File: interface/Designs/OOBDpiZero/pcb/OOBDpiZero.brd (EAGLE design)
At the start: 73.5 x 42 mm, 120 parts, among them IC10 STM32F042CT, IC11 EEPROM24, IC20 GL850G-31, IC3 DS3231, IC4 MC34063-SO, Q2 12MHz, U1 SN65HVD230(SO8), U11 STM32F042CT, U2 SN65HVD230(SO8), U4 SY6280

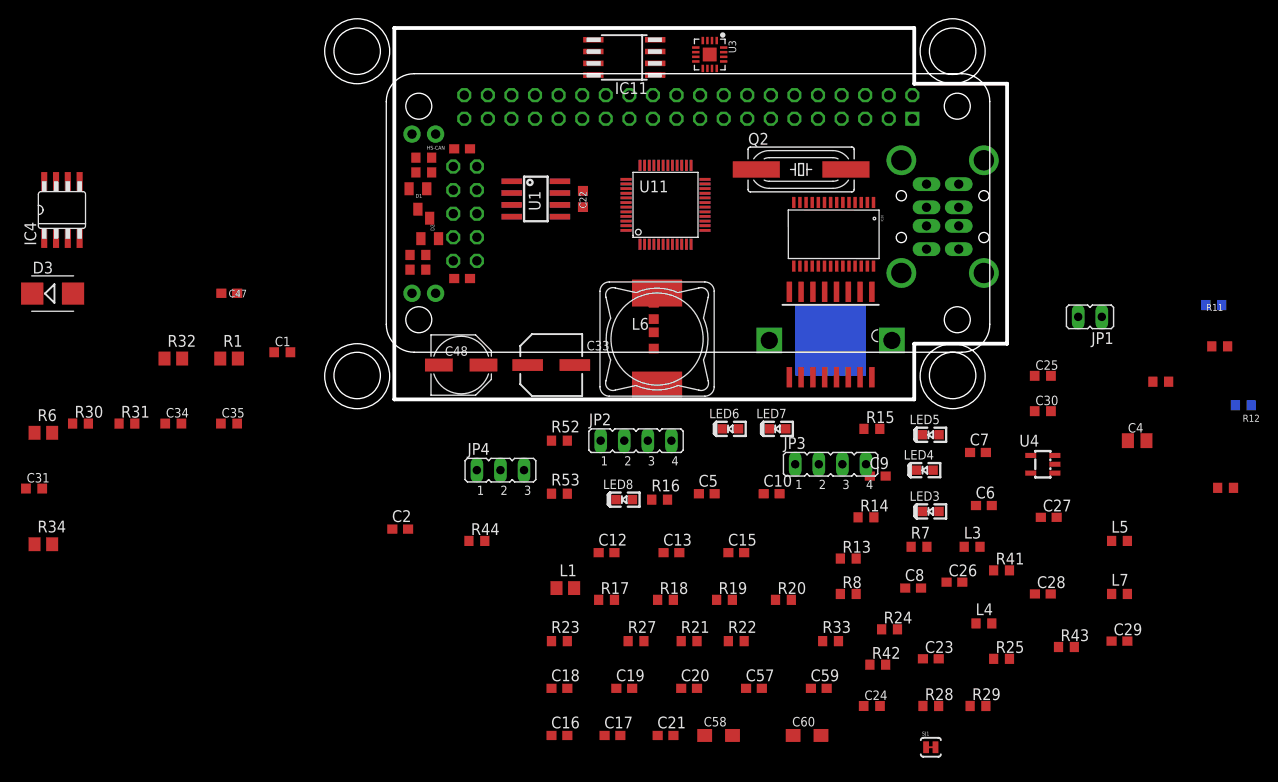
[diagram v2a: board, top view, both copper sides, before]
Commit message: correct last faulty stashed commit
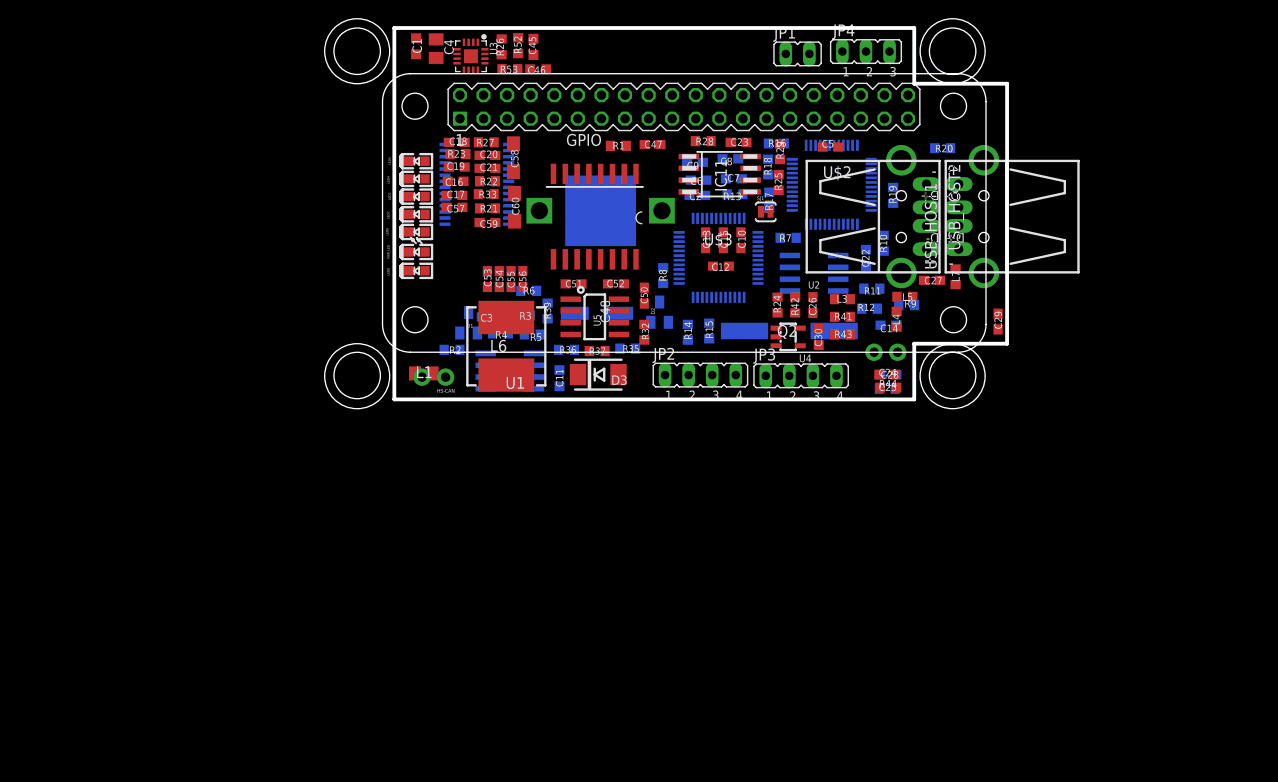
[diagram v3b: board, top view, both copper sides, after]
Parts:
- removed C31: 100n, rcl:C0603K
- removed C33: 47µ/35V, cap-master:SV-D
- removed C34: 100nF, rcl:C0603K
- removed C35: 220pF, rcl:C0603K
- removed IC10, U11: STM32F042CT, micro-stm_v3:LQFP48
- removed IC20: GL850G-31, pimoroni:TSSOP28
- removed IC4: MC34063-SO, mc34063:SO8
- removed JP7: PIZERO_THROUGH_HOLE, pizero:PIZERO_THOUGH_HOLE
- removed OOBD2-CONNECTOR: In-Car Diagnostic, pinhead:2X05/90
- removed R30: 1k2, rcl:R0603
- removed R31: 3k6, rcl:R0603
- removed R34: 1R, rcl:R0805
- added C50: 100nF, rcl:C0603
- added C51: 10nF, rcl:C0603
- added C52: 3.3nF, rcl:C0603
- added C53, C54, C55, C56: 22uF/6.3V, rcl:C0603
- added GPIO: PIZERO_THROUGH_HOLE, pizero:PIZERO_THOUGH_HOLE
- added PWR_LED: LED/Red/0603, DOUBLE-SIDE:LED-0603
- added R35, R39: 2.2k/1%, rcl:R0603
- added R36: 1.05k/1%, rcl:R0603
- added R37: 4.99k/1%, rcl:R0603
- added U$2, U$3: STM32F042CT, micro-stm_v3:LQFP48
- added U$5: GL850G-31, pimoroni:TSSOP28
- added U5: MP1482, OLIMEX_IC:SOIC8
- C48: value 220uF/10V/LOWESR/105C -> 470uF/25V/LOWESR/105C
- D3: value SK24 -> SMBJ16A; device diode:SMB -> OLIMEX_DISCRET:DO214AA
- L6: value 100uH -> 10uH/3.15A/20%; device Inductor-Fastron:PIS4720 -> OLIMEX_DISCRET:8X8MM_3131
- R1, R32, R6: value 1R -> 10k; device rcl:R0805 -> rcl:R0603
- moved R26 91.3 mm to (11.6, 38.0), turned to 270 degrees
- moved C4 86.5 mm to (4.51, 37.8), turned to 270 degrees
- moved R5 74.1 mm to (14.9, 6.99), flipped to the bottom
- moved R4 71.3 mm to (11.4, 7.11), flipped to the bottom
- moved C58 66.0 mm to (12.8, 26.0), turned to 90 degrees
- moved R28 65.6 mm to (33.3, 27.8), turned to 180 degrees
- moved C60 65.0 mm to (13.0, 20.7), turned to 270 degrees
- moved LED3 64.9 mm to (2.41, 21.8)
- moved C21 64.0 mm to (10.0, 24.9), turned to 180 degrees
- moved R29 63.4 mm to (41.5, 26.7), turned to 270 degrees
- moved LED4 63.1 mm to (2.41, 23.7)
- moved LED5 62.7 mm to (2.41, 25.7)
- moved C59 61.6 mm to (10.0, 19.1), turned to 180 degrees
- moved C20 61.4 mm to (10.0, 26.3), turned to 180 degrees
- moved C57 61.0 mm to (6.48, 20.7), turned to 180 degrees
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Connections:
- removed net N$1: IC4.1, IC4.7, IC4.8, R1.1, R32.1, R34.1, R6.1
- new net N$129: PWR_LED.A, R39.2
- new net N$62: R36.1, R37.1, U5.5
- new net N$7: C51.1, U5.1
- new net N$8: C51.2, L6.1, U5.3
- new net N$9: C52.1, U5.6
- net +12V: now also C48.+, D3.C, R32.1, U5.2; no longer C33.+, C34.1, IC4.6, OOBD2-CONNECTOR.10, R1.2, R32.2, R34.2, R6.2
- net +3V3: now also GPIO.1, GPIO.17, R1.1, R6.1, U$2.1, U$2.24, U$2.36, U$2.48, U$2.9, U$3.1, U$3.24, U$3.36, U$3.48, U$3.9; no longer IC10.1, IC10.24, IC10.36, IC10.48, IC10.9, JP7.1, JP7.17, U11.1, U11.24, U11.36, U11.48, U11.9
- net +5V: now also C53.1, C54.1, C55.1, C56.1, GPIO.2, GPIO.4, L6.2, R37.2, R39.1, U$5.23; no longer C31.1, C48.+, IC20.23, JP7.2, JP7.4, L6.P$1, R31.2
- net AUD_BCLK: now also GPIO.18; no longer JP7.18
- net AUD_DIN: now also GPIO.21; no longer JP7.21
- net AUD_LRCLK: now also GPIO.19; no longer JP7.19
- net AUD_SD_MODE: now also GPIO.29; no longer JP7.29
- net GND: now also C50.2, C53.2, C54.2, C55.2, C56.2, GPIO.14, GPIO.20, GPIO.25, GPIO.30, GPIO.34, GPIO.39, GPIO.6, GPIO.9, PWR_LED.C, R35.2, R36.2, U$2.23, U$2.35, U$2.47, U$2.8, U$3.23, U$3.35, U$3.47, U$3.8, U$5.14, U$5.15, U5.4; no longer C31.2, C33.-, C34.2, C35.2, IC10.23, IC10.35, IC10.47, IC10.8, IC20.14, IC20.15, IC4.4, JP7.14, JP7.20, JP7.25, JP7.30, JP7.34, JP7.39, JP7.6, JP7.9, OOBD2-CONNECTOR.3, R30.2, U11.23, U11.35, U11.47, U11.8
- net HS-CAN_H: no longer OOBD2-CONNECTOR.7
- net HS-CAN_L: no longer OOBD2-CONNECTOR.6
- net HS-CAN_RS: now also GPIO.35; no longer JP7.35
- net HS-CAN_RXD: now also U$3.45; no longer IC10.45
- net HS-CAN_TXD: now also U$3.46; no longer IC10.46
- net ID_SC: now also GPIO.28; no longer JP7.28
- net ID_SD: now also GPIO.27; no longer JP7.27
- net MS-CAN_H: no longer OOBD2-CONNECTOR.1
- net MS-CAN_L: no longer OOBD2-CONNECTOR.2
- net MS-CAN_RS: now also GPIO.36; no longer JP7.36
- net MS-CAN_RXD: now also U$2.45; no longer U11.45
- net MS-CAN_TXD: now also U$2.46; no longer U11.46
- net N$11: now also C52.2, R35.1; no longer C35.1, IC4.3
- net N$13: now also U$3.10; no longer IC10.10
- net N$14: now also U$3.11; no longer IC10.11
- net N$15: now also U$3.44; no longer IC10.44
- net N$16: now also U$3.12; no longer IC10.12
- net N$20: now also U$3.7; no longer IC10.7
- net N$21: now also U$2.44; no longer U11.44
- net N$22: now also U$2.10; no longer U11.10
- net N$23: now also U$2.11; no longer U11.11
- net N$24: now also U$2.12; no longer U11.12
- net N$28: now also U$2.7; no longer U11.7
- net N$29: now also U$5.7; no longer IC20.7
- net N$31: now also U$5.6; no longer IC20.6
- net N$33: now also U$5.16, U$5.24; no longer IC20.16, IC20.24
- net N$34: now also U$5.18; no longer IC20.18
- net N$35: now also U$5.17; no longer IC20.17
- net N$36: now also U$5.13; no longer IC20.13
- net N$39: now also U$5.1, U$5.10, U$5.5; no longer IC20.1, IC20.10, IC20.5
- net N$4: now also C50.1, U5.8; no longer IC4.5, R30.1, R31.1
- net N$40: now also U$5.4; no longer IC20.4
- net N$6: now also R32.2, U5.7; no longer D3.C, IC4.2, L6.P$2
- net PP22: now also U$5.26; no longer IC20.26
- net PP23: now also U$5.25; no longer IC20.25
- net SCL: now also GPIO.5, R1.2; no longer JP7.5
- net SDA: now also GPIO.3, R6.2; no longer JP7.3
- net SWCLK: now also U$2.37, U$3.37; no longer IC10.37, U11.37
- net SWDIO: now also U$2.34, U$3.34; no longer IC10.34, U11.34
- net UART0_RXD: now also GPIO.10; no longer JP7.10
- net UART0_TXD: now also GPIO.8; no longer JP7.8
- net USB0_DM: now also U$3.32, U$5.27; no longer IC10.32, IC20.27
- net USB0_DP: now also U$3.33, U$5.28; no longer IC10.33, IC20.28
- net USB1_DM: now also U$2.32, U$5.2; no longer IC20.2, U11.32
- net USB1_DP: now also U$2.33, U$5.3; no longer IC20.3, U11.33
- net USB2_DM: now also U$5.8; no longer IC20.8
- net USB2_DP: now also U$5.9; no longer IC20.9
- net USB3_DM: now also U$5.11; no longer IC20.11
- net USB3_DP: now also U$5.12; no longer IC20.12
- net USB_CE: now also GPIO.31; no longer JP7.31
- net USB_VBUS: now also GPIO.32; no longer JP7.32

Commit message: - replace internal USB-A with micro-USB connector - connect "old" internal USB interface to micro-USB connector to either use as 5V power supply or USB-HUB input as external AddOn extension - add missing 3V3 LDO (optional) for use without Pi Zero (W)
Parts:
- added C31, C32: 10uF/6.3V, rcl:C0603
- added IC1: LM1117MPX-3.3, lm1117:SOT223
- added R30, R31: NI(0R), resistor:R0603
- added R34: NI(0R), resistor:R0805
- USB_HOST2: device OLIMEX_CONNECTORS:USB_PN87520_DEV_PTH -> con-molex-usb:47589-0001
- moved USB_HOST2 9.55 mm to (64.1, 20.3), flipped to the bottom, turned to 0 degrees
- moved USB_HOST1 2.62 mm to (61.0, 20.3)
- moved L7 2.62 mm to (57.9, 12.6)
- moved C27 2.54 mm to (55.4, 12.8)
- moved R20 1.91 mm to (57.1, 27.1)
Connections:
- new net N$1: C27.1, C29.1, L5.1, R34.1
- net +3V3: now also C32.1, IC1.2, IC1.TAB
- net +5V: now also C31.1, IC1.3, R34.2
- net GND: now also C31.2, C32.2, IC1.1
- net N$47: no longer C27.1, C29.1, L5.1
- net N$49: now also USB_HOST2.5; no longer USB_HOST2.P$1, USB_HOST2.P$2
- net PP22: now also R31.2
- net PP23: now also R30.2
- net USB3_DM: now also R30.1
- net USB3_DP: now also R31.1

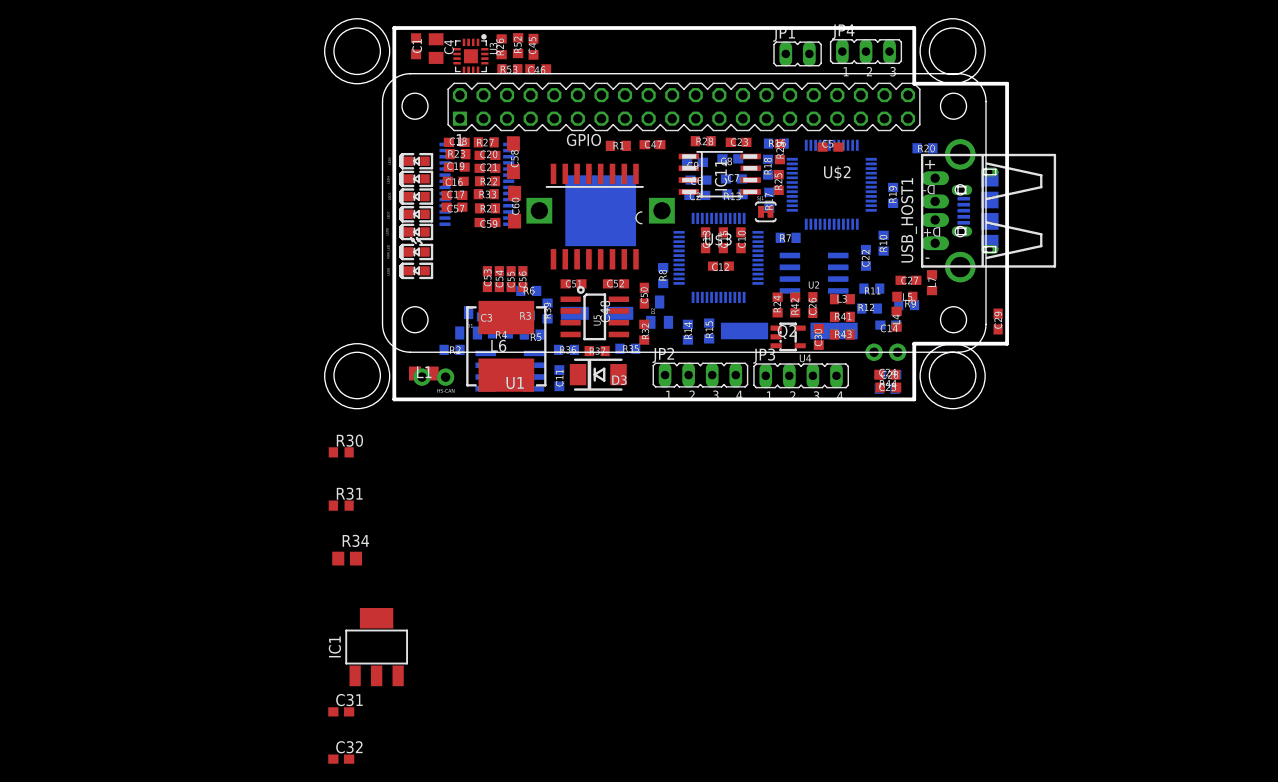
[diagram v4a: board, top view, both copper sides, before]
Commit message: PP22/PP23 Pi-Zero USB connection placed and locked add missing OOBD default OBD2-Connector
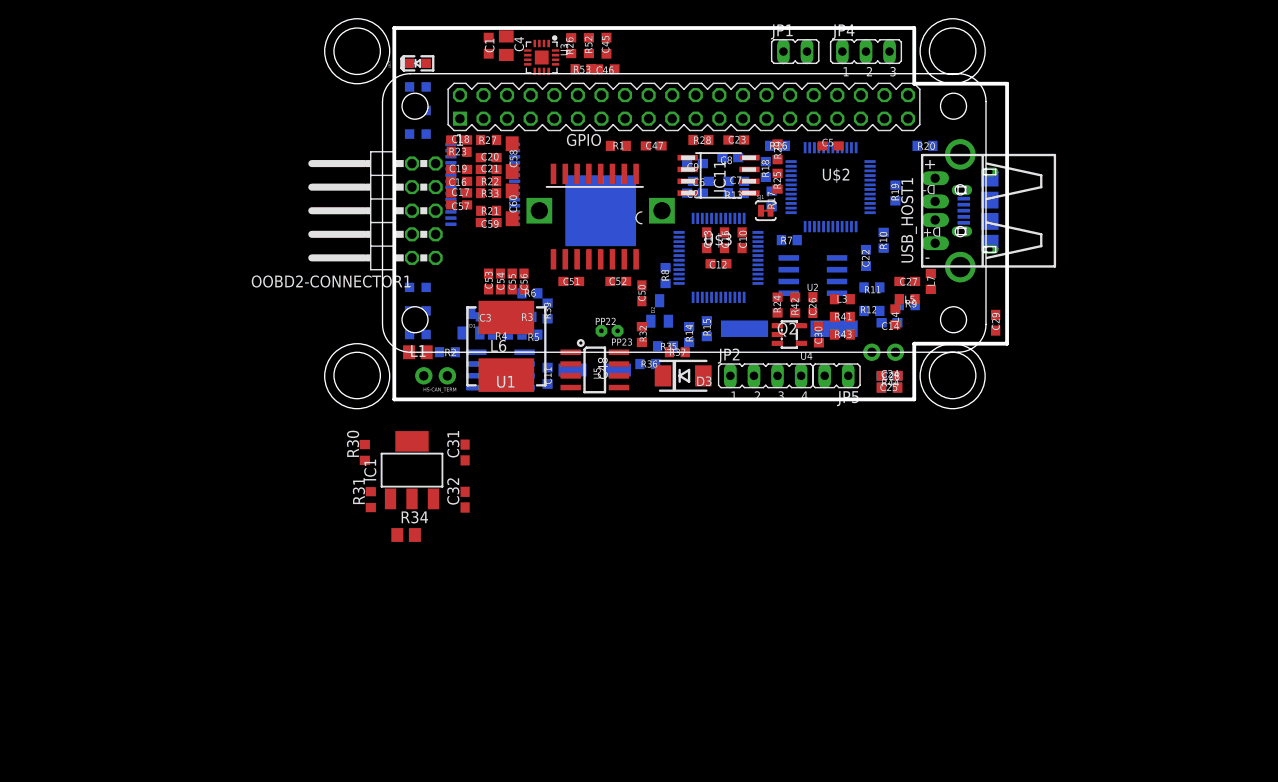
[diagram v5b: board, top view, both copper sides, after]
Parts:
- removed HS-CAN, MS-CAN: OPEN, SparkFun:1X02
- removed JP3: (no value), jumper:JP4
- added HS-CAN_TERM, MS-CAN_TERM: OPEN, SparkFun:1X02
- added JP5: (no value), jumper:JP1
- added OOBD2-CONNECTOR1: In-Car Diagnostic, pinhead:2X05/90
- added PP22, PP23: PTR1PAD1-11, testpad:P1-11
- moved C31 31.0 mm to (7.62, -5.71), turned to 90 degrees
- moved C32 31.0 mm to (7.62, -10.8), turned to 90 degrees
- moved IC1 19.4 mm to (1.91, -7.62)
- moved LED7 16.3 mm to (2.54, 36.2)
- moved D3 9.14 mm to (31.1, 2.54)
- moved R36 8.89 mm to (27.3, 3.81)
- moved R37 8.64 mm to (30.5, 5.08)
- moved LED5 8.00 mm to (2.54, 33.7), flipped to the bottom
- moved C45 7.88 mm to (22.9, 38.1)
- moved R53 7.87 mm to (20.3, 35.6)
- moved C1 7.81 mm to (10.2, 38.1)
- moved U3 7.62 mm to (15.9, 36.8)
- moved R52 7.62 mm to (21.0, 38.1)
- moved C4 7.56 mm to (12.1, 38.1)
- moved R26 7.49 mm to (19.1, 38.1)
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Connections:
- net +12V: now also OOBD2-CONNECTOR1.10
- net +3V3: no longer JP3.1
- net GND: now also OOBD2-CONNECTOR1.3; no longer JP3.4
- net HS-CAN_H: now also OOBD2-CONNECTOR1.7
- net HS-CAN_L: now also HS-CAN_TERM.1, OOBD2-CONNECTOR1.6; no longer HS-CAN.1
- net MS-CAN_H: now also OOBD2-CONNECTOR1.1
- net MS-CAN_L: now also MS-CAN_TERM.1, OOBD2-CONNECTOR1.2; no longer MS-CAN.1
- net N$30: now also HS-CAN_TERM.2; no longer HS-CAN.2
- net N$32: now also MS-CAN_TERM.2; no longer MS-CAN.2
- net PP22: now also PP22.P$1
- net PP23: now also PP23.P$1
- net SWCLK: now also JP5.2; no longer JP3.3
- net SWDIO: now also JP5.1; no longer JP3.2

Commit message: - lock position for OOBD2 connector - place all parts on PCB but minor placing optimization necessary as preparation for autorouter
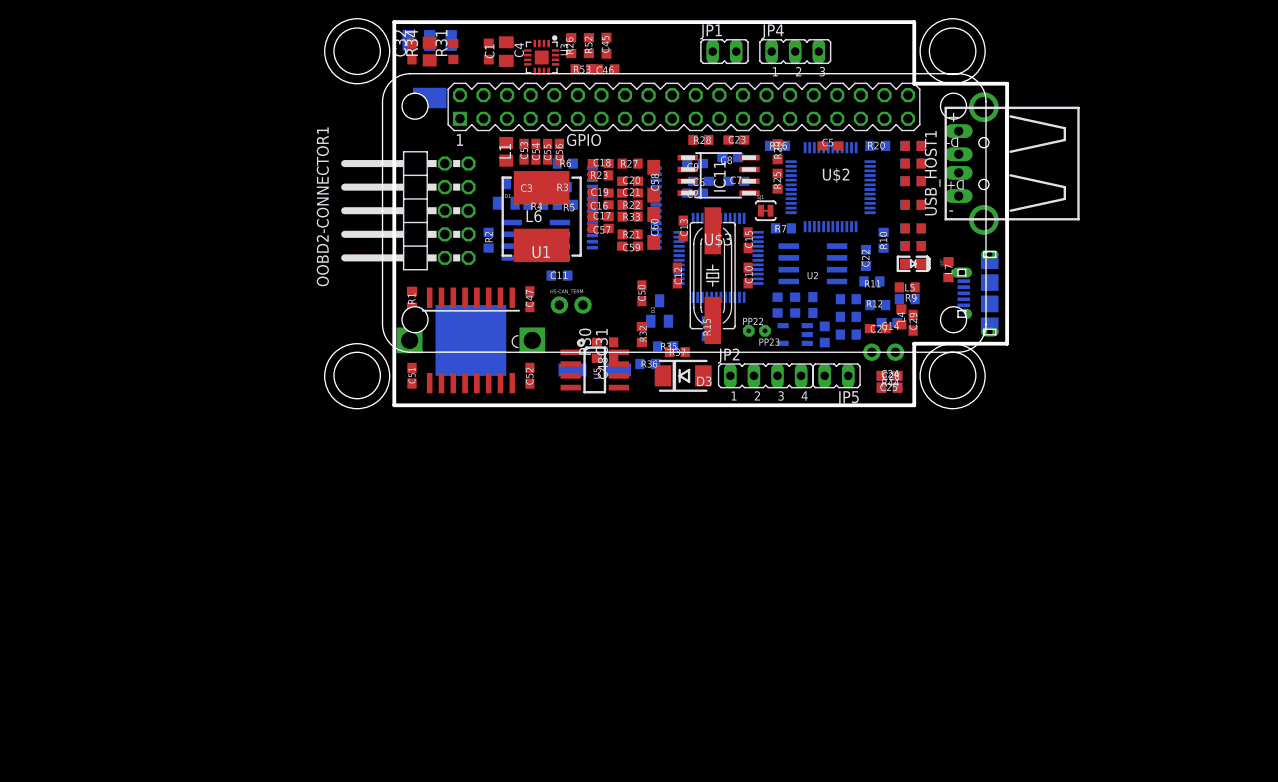
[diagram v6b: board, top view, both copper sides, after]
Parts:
- JP1: value (none) -> Audio-Out
- JP2: value (none) -> Prog0_IO
- JP4: value (none) -> UART
- JP5: value (none) -> Prog2_IO
- U3: value (none) -> MAX98357
- moved LED7 57.5 mm to (55.9, 14.6), turned to 180 degrees
- moved PWR_LED 54.6 mm to (55.9, 21.0)
- moved LED8 54.2 mm to (55.9, 16.5)
- moved LED4 53.9 mm to (55.9, 23.5)
- moved LED5 53.7 mm to (55.9, 27.3)
- moved LED6 53.7 mm to (55.9, 18.4)
- moved LED3 53.4 mm to (55.9, 25.4)
- moved R34 52.1 mm to (3.81, 37.5), turned to 90 degrees
- moved R31 49.1 mm to (6.35, 37.5)
- moved C32 48.6 mm to (1.91, 37.5)
- moved IC1 43.2 mm to (3.81, 35.6), flipped to the bottom, turned to 180 degrees
- moved R39 41.0 mm to (55.9, 21.0), flipped to the top, turned to 0 degrees
- moved R14 31.5 mm to (55.9, 27.3), flipped to the top, turned to 0 degrees
- moved R8 29.3 mm to (55.9, 25.4), flipped to the top, turned to 0 degrees
- moved R1 27.7 mm to (1.91, 10.8), turned to 90 degrees
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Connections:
- removed net USB3_DM: R30.1, U$5.11, USB_HOST2.2
- removed net USB3_DP: R31.1, U$5.12, USB_HOST2.3
- new net N$38: R30.1, USB_HOST2.2
- new net N$43: R31.1, USB_HOST2.3
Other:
- outline, holes or cut-outs redrawn
